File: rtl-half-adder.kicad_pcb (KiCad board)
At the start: 2 copper layers, 37 parts, among them Q1 Q_NPN_EBC, Q10 Q_NPN_EBC, Q11 Q_NPN_EBC, Q12 Q_NPN_EBC, Q13 Q_NPN_EBC, Q2 Q_NPN_EBC, Q3 Q_NPN_EBC, Q4 Q_NPN_EBC, Q5 Q_NPN_EBC, Q6 Q_NPN_EBC, Q7 Q_NPN_EBC, Q8 Q_NPN_EBC, Q9 Q_NPN_EBC, SW1 SW_DIP_x02

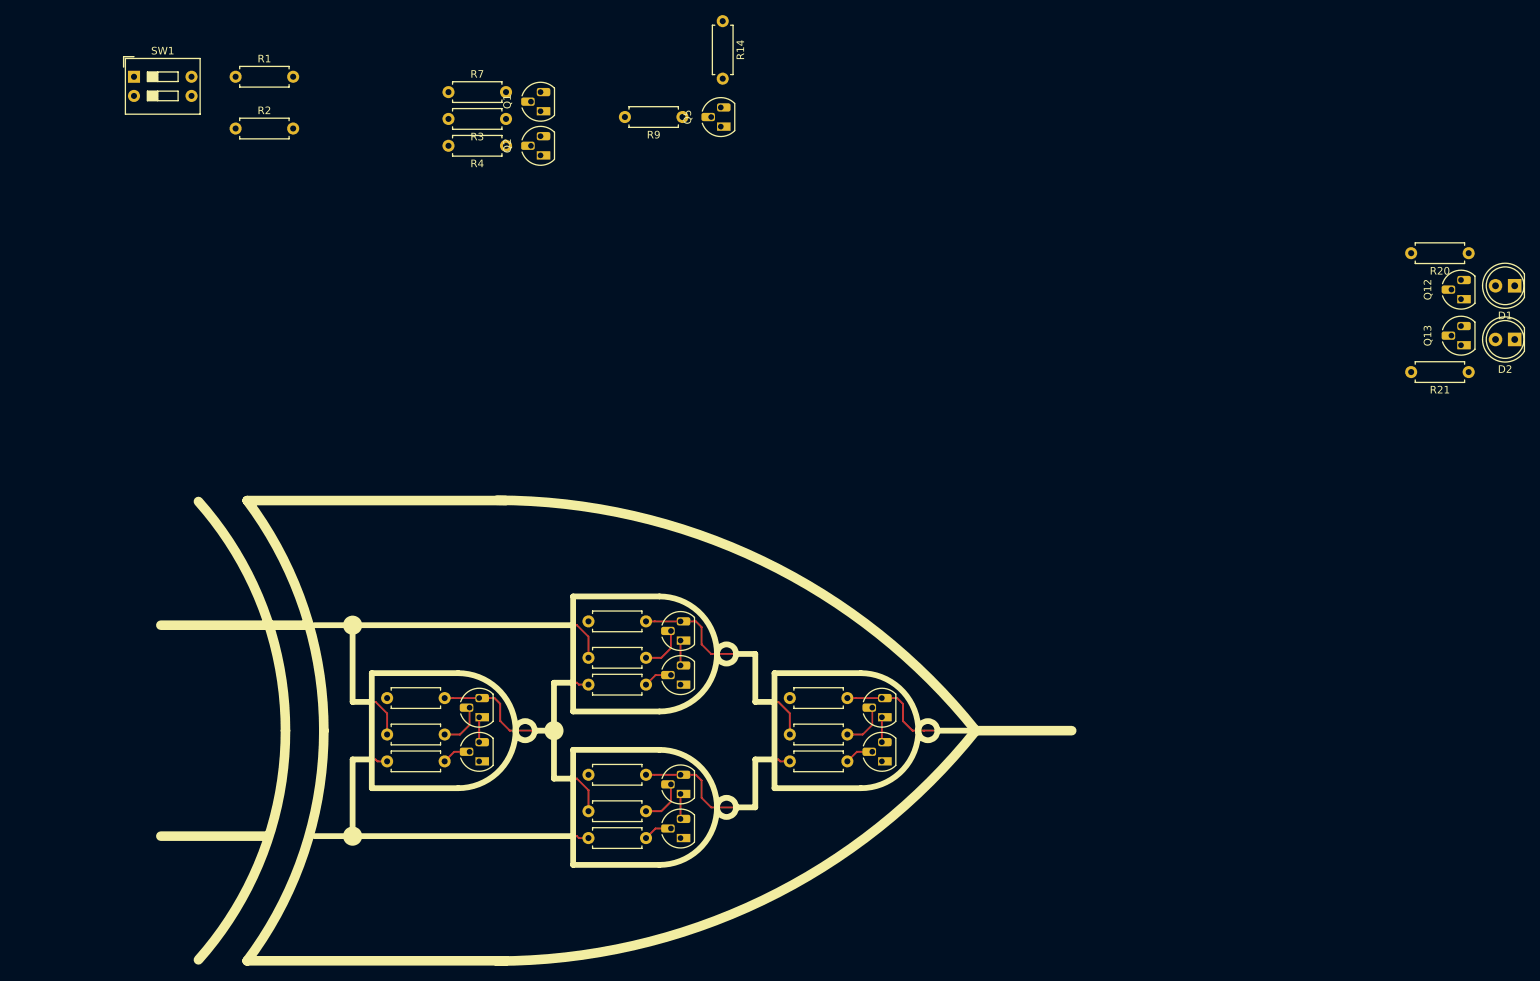
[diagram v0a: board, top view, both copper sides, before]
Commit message: through hole components and silk screen done
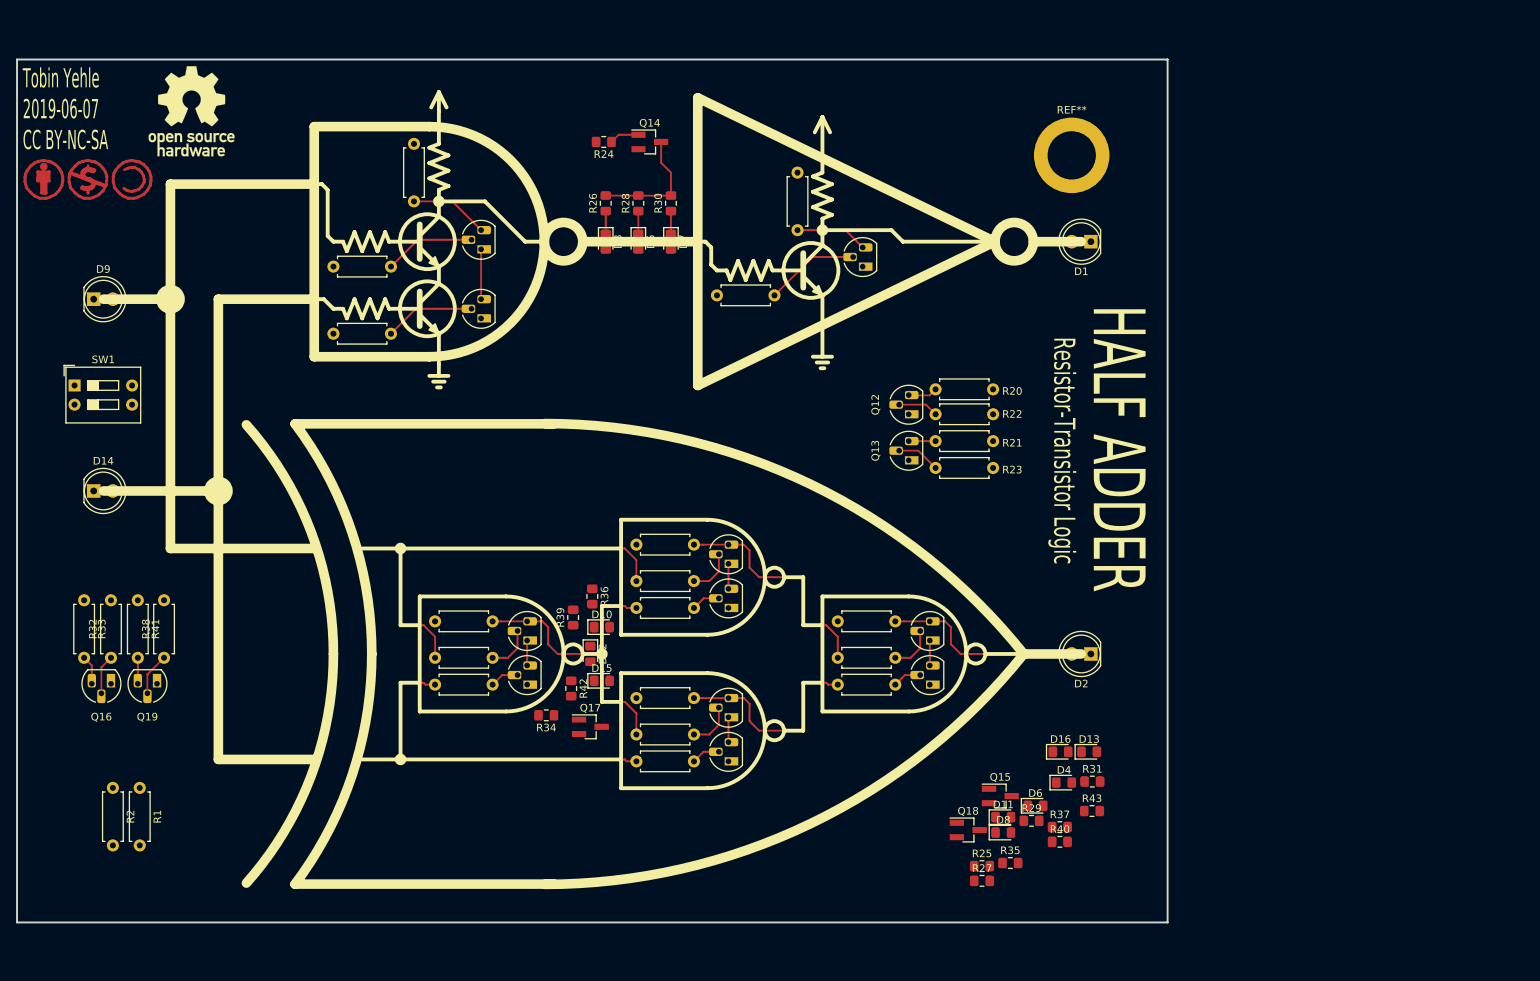
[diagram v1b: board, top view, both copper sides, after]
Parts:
- added D10: LED, LED_SMD:LED_0805_2012Metric_Pad1.15x1.40mm_HandSolder, F.Cu at (128.3, 113.3)
- added D11: LED, LED_SMD:LED_0805_2012Metric_Pad1.15x1.40mm_HandSolder, F.Cu at (181.4, 138.5)
- added D12: LED, LED_SMD:LED_0805_2012Metric_Pad1.15x1.40mm_HandSolder, F.Cu at (126.7, 116.8)
- added D13: LED, LED_SMD:LED_0805_2012Metric_Pad1.15x1.40mm_HandSolder, F.Cu at (192.8, 129.8)
- added D14: LED, LED_THT:LED_D5.0mm, F.Cu at (61.0, 95.2)
- added D15: LED, LED_SMD:LED_0805_2012Metric_Pad1.15x1.40mm_HandSolder, F.Cu at (128.3, 120.4)
- added D16: LED, LED_SMD:LED_0805_2012Metric_Pad1.15x1.40mm_HandSolder, F.Cu at (189.0, 129.8)
- added D3: LED, LED_SMD:LED_0805_2012Metric_Pad1.15x1.40mm_HandSolder, F.Cu at (128.8, 62.2)
- added D4: LED, LED_SMD:LED_0805_2012Metric_Pad1.15x1.40mm_HandSolder, F.Cu at (189.5, 133.9)
- added D5: LED, LED_SMD:LED_0805_2012Metric_Pad1.15x1.40mm_HandSolder, F.Cu at (133.1, 62.2)
- added D6: LED, LED_SMD:LED_0805_2012Metric_Pad1.15x1.40mm_HandSolder, F.Cu at (185.7, 136.9)
- added D7: LED, LED_SMD:LED_0805_2012Metric_Pad1.15x1.40mm_HandSolder, F.Cu at (137.4, 62.2)
- added D8: LED, LED_SMD:LED_0805_2012Metric_Pad1.15x1.40mm_HandSolder, F.Cu at (181.4, 140.5)
- added D9: LED, LED_THT:LED_D5.0mm, F.Cu at (61.0, 69.8)
- added Q14: Q_NPN_BEC, Package_TO_SOT_SMD:SOT-23_Handsoldering, F.Cu at (134.6, 49.0)
- added Q15: Q_NPN_BEC, Package_TO_SOT_SMD:SOT-23_Handsoldering, F.Cu at (181.0, 135.7)
- added Q16: Q_NPN_EBC, Package_TO_SOT_THT:TO-92_HandSolder, F.Cu at (63.2, 120.8)
- added Q17: Q_NPN_BEC, Package_TO_SOT_SMD:SOT-23_Handsoldering, F.Cu at (126.7, 126.5)
- added Q18: Q_NPN_BEC, Package_TO_SOT_SMD:SOT-23_Handsoldering, F.Cu at (176.8, 140.2)
- added Q19: Q_NPN_EBC, Package_TO_SOT_THT:TO-92_HandSolder, F.Cu at (69.3, 120.8)
- added R22: 10k, Resistor_THT:R_Axial_DIN0207_L6.3mm_D2.5mm_P7.62mm_Horizontal, F.Cu at (172.5, 85.1)
- added R23: 10k, Resistor_THT:R_Axial_DIN0207_L6.3mm_D2.5mm_P7.62mm_Horizontal, F.Cu at (172.5, 92.2)
- added R24: 10k, Resistor_SMD:R_0805_2012Metric_Pad1.15x1.40mm_HandSolder, F.Cu at (128.5, 49.0)
- added R25: 10k, Resistor_SMD:R_0805_2012Metric_Pad1.15x1.40mm_HandSolder, F.Cu at (178.6, 144.9)
- added R26: 68, Resistor_SMD:R_0805_2012Metric_Pad1.15x1.40mm_HandSolder, F.Cu at (128.8, 57.1)
- added R27: 68, Resistor_SMD:R_0805_2012Metric_Pad1.15x1.40mm_HandSolder, F.Cu at (178.6, 146.9)
- added R28: 68, Resistor_SMD:R_0805_2012Metric_Pad1.15x1.40mm_HandSolder, F.Cu at (133.1, 57.1)
- added R29: 68, Resistor_SMD:R_0805_2012Metric_Pad1.15x1.40mm_HandSolder, F.Cu at (185.2, 138.9)
- added R30: 68, Resistor_SMD:R_0805_2012Metric_Pad1.15x1.40mm_HandSolder, F.Cu at (137.4, 57.1)
- added R31: 68, Resistor_SMD:R_0805_2012Metric_Pad1.15x1.40mm_HandSolder, F.Cu at (193.2, 133.7)
- added R32: 10k, Resistor_THT:R_Axial_DIN0207_L6.3mm_D2.5mm_P7.62mm_Horizontal, F.Cu at (63.2, 117.3)
- added R33: 68, Resistor_THT:R_Axial_DIN0207_L6.3mm_D2.5mm_P7.62mm_Horizontal, F.Cu at (59.7, 109.7)
- added R34: 10k, Resistor_SMD:R_0805_2012Metric_Pad1.15x1.40mm_HandSolder, F.Cu at (120.9, 125.0)
- added R35: 10k, Resistor_SMD:R_0805_2012Metric_Pad1.15x1.40mm_HandSolder, F.Cu at (182.4, 144.5)
- added R36: 68, Resistor_SMD:R_0805_2012Metric_Pad1.15x1.40mm_HandSolder, F.Cu at (127.0, 109.2)
- added R37: 68, Resistor_SMD:R_0805_2012Metric_Pad1.15x1.40mm_HandSolder, F.Cu at (188.9, 139.8)
- added R38: 10k, Resistor_THT:R_Axial_DIN0207_L6.3mm_D2.5mm_P7.62mm_Horizontal, F.Cu at (70.3, 117.3)
- added R39: 68, Resistor_SMD:R_0805_2012Metric_Pad1.15x1.40mm_HandSolder, F.Cu at (124.5, 112.0)
- added R40: 68, Resistor_SMD:R_0805_2012Metric_Pad1.15x1.40mm_HandSolder, F.Cu at (188.9, 141.7)
- added R41: 68, Resistor_THT:R_Axial_DIN0207_L6.3mm_D2.5mm_P7.62mm_Horizontal, F.Cu at (66.8, 109.7)
- added R42: 68, Resistor_SMD:R_0805_2012Metric_Pad1.15x1.40mm_HandSolder, F.Cu at (124.2, 121.4)
- added R43: 68, Resistor_SMD:R_0805_2012Metric_Pad1.15x1.40mm_HandSolder, F.Cu at (193.2, 137.6)
- added REF**: OSHW-Logo_11.4x12mm_SilkScreen, Symbol:OSHW-Logo_11.4x12mm_SilkScreen, F.Cu at (73.9, 45.0)
- added REF**: MountingHole_6.4mm_M6_ISO14580_Pad, MountingHole:MountingHole_6.4mm_M6_ISO14580_Pad, F.Cu at (190.5, 50.8)
- added REF**: Symbol_CC-Attribution_CopperTop_Small, Symbol:Symbol_CC-Attribution_CopperTop_Small, F.Cu at (54.4, 54.0)
- added REF**: Symbol_CC-Noncommercial_CopperTop_Small, Symbol:Symbol_CC-Noncommercial_CopperTop_Small, F.Cu at (60.2, 54.0)
- added REF**: Symbol_CC-ShareAlike_CopperTop_Small, Symbol:Symbol_CC-ShareAlike_CopperTop_Small, F.Cu at (66.0, 54.0)
- R10, R11, R12, R13, R17, R18, R3, R4, R5, R6, R9: value 1k -> 10k
- moved R1 95.0 mm to (67.1, 134.6), turned to 270 degrees
- moved R2 88.8 mm to (63.5, 134.6), turned to 270 degrees
- moved Q12 74.7 mm to (168.9, 85.1)
- moved Q13 74.7 mm to (168.9, 91.2)
- moved D2 69.9 mm to (193.0, 116.8)
- moved R20 65.5 mm to (180.1, 81.8)
- moved R21 63.7 mm to (180.1, 88.6)
- moved D1 56.4 mm to (193.0, 62.2)
- moved SW1 41.6 mm to (58.4, 81.3)
- moved R4 29.2 mm to (100.3, 74.4)
- moved R9 26.6 mm to (151.1, 69.3)
- moved Q5 26.4 mm to (162.8, 65.5)
- moved R3 24.8 mm to (100.3, 65.5)
- moved Q2 23.0 mm to (112.3, 72.4)
- moved R14 22.4 mm to (154.2, 53.1)
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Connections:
- net Net-(Q1-Pad3) renamed NAND1
- net Net-(Q3-Pad3) renamed XOR1
- net Net-(Q6-Pad3) renamed XOR2
- net Net-(Q8-Pad3) renamed XOR3
- D1 pad 2: Net-(D1-Pad2) -> VCC
- D2 pad 2: Net-(D2-Pad2) -> VCC
- Q10 pad 3: Net-(Q10-Pad3) -> SUM
- Q12 pad 1: Net-(D1-Pad2) -> GND
- Q12 pad 3: VCC -> Net-(Q12-Pad3)
- Q13 pad 1: Net-(D2-Pad2) -> GND
- Q13 pad 2: Net-(Q10-Pad3) -> Net-(Q13-Pad2)
- Q13 pad 3: VCC -> Net-(Q13-Pad3)
- Q5 pad 3: Net-(Q12-Pad2) -> CARRY
- R1 pad 1: Net-(R1-Pad1) -> B
- R10 pad 2: Net-(R1-Pad1) -> A
- R13 pad 2: Net-(R13-Pad2) -> B
- R14 pad 2: Net-(Q12-Pad2) -> CARRY
- R19 pad 2: Net-(Q10-Pad3) -> SUM
- R2 pad 1: Net-(R13-Pad2) -> A
- R20 pad 2: GND -> Net-(Q12-Pad3)
- R21 pad 2: GND -> Net-(Q13-Pad3)
- R3 pad 2: Net-(R1-Pad1) -> A
- R4 pad 2: Net-(R13-Pad2) -> B
- R5 pad 2: Net-(R1-Pad1) -> A
- R6 pad 2: Net-(R13-Pad2) -> B
- SW1 pad 3: Net-(R13-Pad2) -> B
- SW1 pad 4: Net-(R1-Pad1) -> A
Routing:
- net Net-(R1-Pad1): track 51.9 -> 0.00 mm
- net Net-(R13-Pad2): track 45.3 -> 0.00 mm
- net A: track 0.00 -> 41.1 mm
- net B: track 0.00 -> 34.5 mm
- net SUM: track 0.00 -> 21.4 mm
- net Net-(Q10-Pad3): track 21.4 -> 0.00 mm
- net Net-(Q14-Pad3): track 0.00 -> 16.3 mm
- net XOR1: track 42.2 -> 29.3 mm
- net Net-(Q5-Pad2): track 0.00 -> 12.5 mm
- net Net-(Q1-Pad2): track 0.00 -> 12.1 mm
- net Net-(Q2-Pad2): track 0.00 -> 12.0 mm
- net NAND1: track 0.00 -> 10.5 mm
- net CARRY: track 0.00 -> 9.58 mm
- net XOR2: track 31.4 -> 24.6 mm
- net XOR3: track 28.0 -> 21.3 mm
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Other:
- board outline added: 152.4 x 114.3 mm
- board text added: "HALF ADDER"
- board text added: "Resistor-Transistor Logic"
- board text added: "Tobin Yehle 2019-06-07 CC BY-NC-SA"

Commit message: update footprints for smd leds
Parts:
- D10, D11, D12, D13, D15, D16, D3, D4, D5, D6, D7, D8: footprint LED_SMD:LED_0805_2012Metric_Pad1.15x1.40mm_HandSolder -> --Project:LED_1206_3216Metric_ReverseMount_Hole1.8x2.4mm

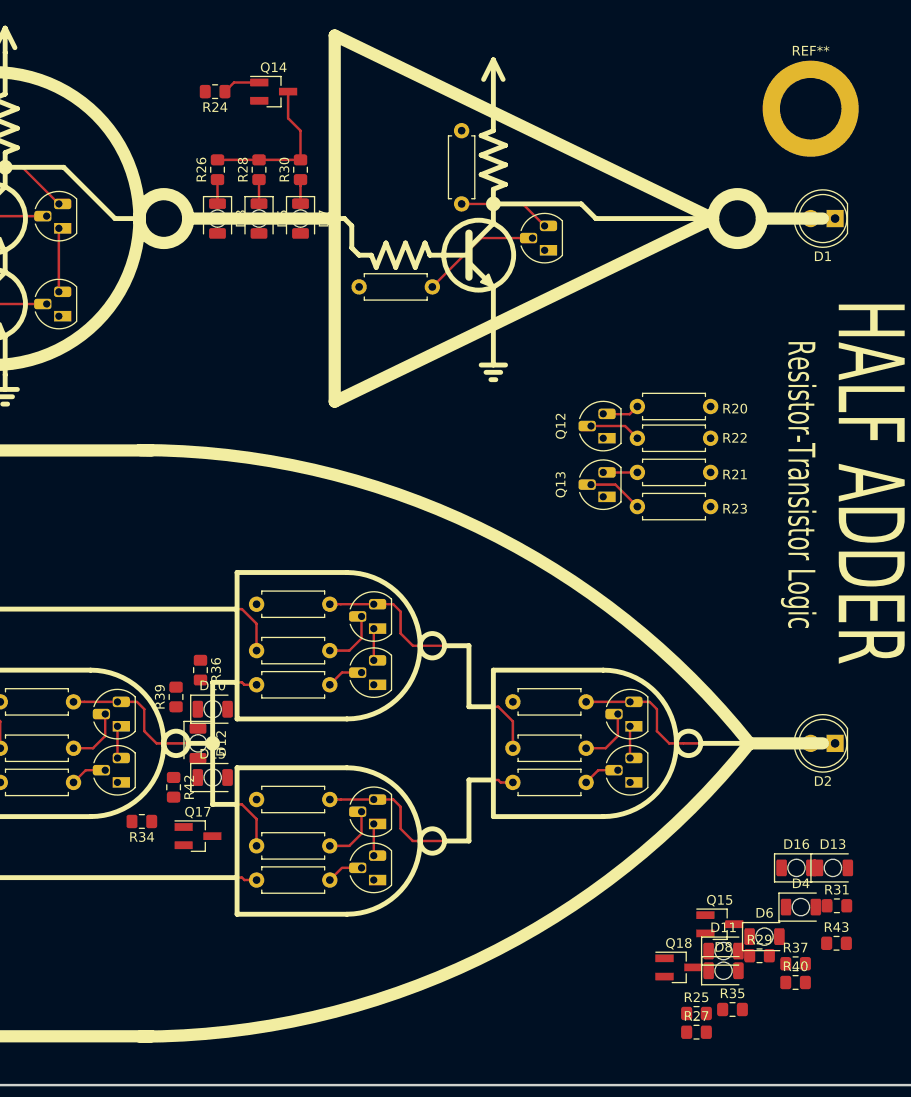
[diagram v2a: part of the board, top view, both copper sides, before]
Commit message: inter gate led layout done
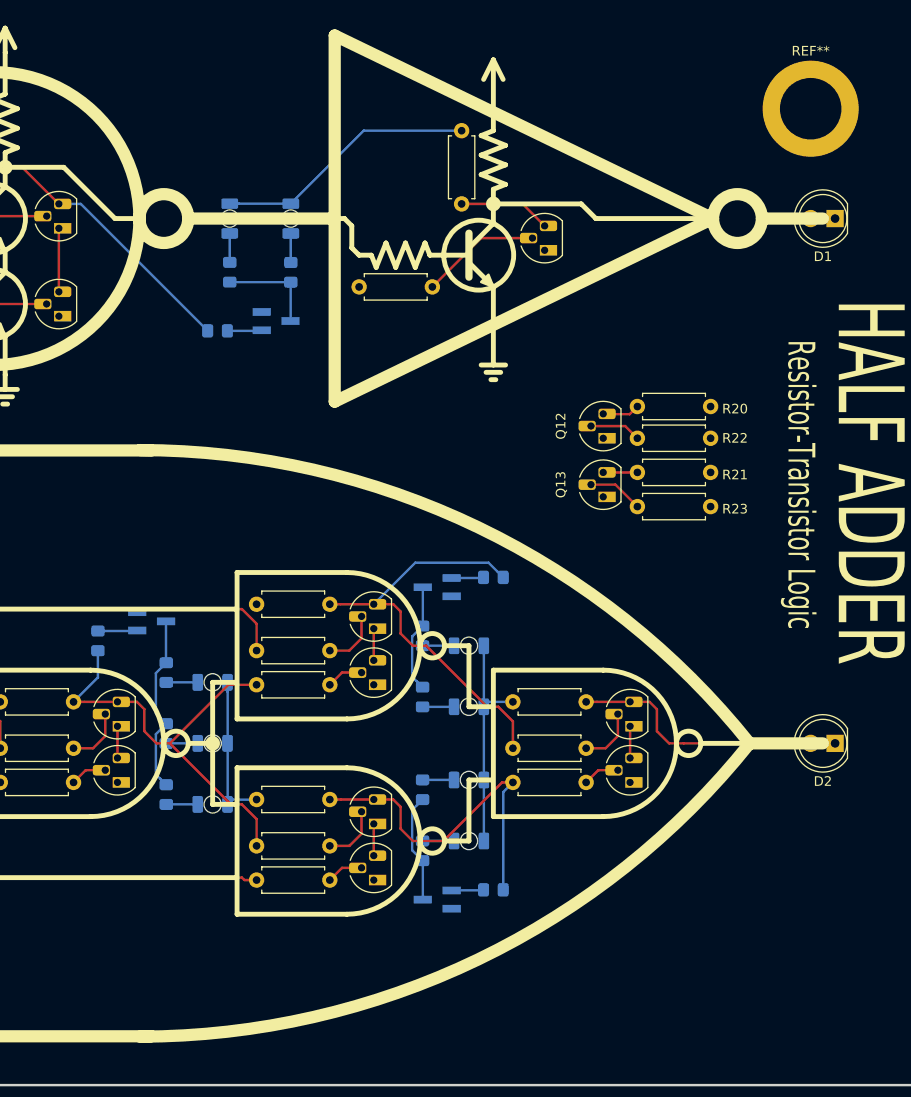
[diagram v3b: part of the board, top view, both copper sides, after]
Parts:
- removed D16, D7, D8: LED, --Project:LED_1206_3216Metric_ReverseMount_Hole1.8x2.4mm
- removed R30, R31, R43: 68, Resistor_SMD:R_0805_2012Metric_Pad1.15x1.40mm_HandSolder
- D10, D11, D12, D13, D15, D3, D4, D5, D6, Q14, Q15, Q17, Q18, R24, R25, R26, R27, R28, R29, R34, R35, R36, R37, R39, R40, R42: moved to B.Cu
- moved R27 50.1 mm to (150.1, 105.7), turned to 90 degrees
- moved R25 50.1 mm to (157.5, 99.6)
- moved Q15 45.8 mm to (151.6, 100.6), turned to 180 degrees
- moved R29 44.2 mm to (150.1, 112.0), turned to 90 degrees
- moved D4 44.0 mm to (154.9, 106.7)
- moved R40 43.7 mm to (150.1, 121.7), turned to 270 degrees
- moved R37 40.6 mm to (150.1, 128.0), turned to 270 degrees
- moved D13 39.0 mm to (154.9, 120.7)
- moved D6 39.0 mm to (154.9, 113.0)
- moved D11 28.9 mm to (154.9, 127.0)
- moved R35 27.8 mm to (157.5, 132.1)
- moved Q18 26.1 mm to (151.6, 133.1), turned to 180 degrees
- moved R24 24.9 mm to (128.8, 73.9)
- moved Q14 23.9 mm to (134.9, 72.9)
- moved Q17 22.9 mm to (121.9, 104.1)
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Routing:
- net VCC: track 0.00 -> 66.8 mm
- net NAND1: track 10.5 -> 31.4 mm
- net XOR2: track 24.6 -> 44.1 mm
- net Net-(Q17-Pad3): track 0.00 -> 18.8 mm
- net XOR1: track 29.3 -> 46.2 mm
- net XOR3: track 21.3 -> 36.3 mm
- net Net-(Q18-Pad3): track 0.00 -> 11.3 mm
- net Net-(Q15-Pad3): track 0.00 -> 11.3 mm
- net Net-(Q14-Pad3): track 16.3 -> 10.4 mm
- net Net-(Q17-Pad1): track 0.00 -> 4.11 mm
- net Net-(Q15-Pad1): track 0.00 -> 3.34 mm
- net Net-(Q18-Pad1): track 0.00 -> 3.34 mm
- net Net-(D15-Pad1): track 0.00 -> 3.28 mm
- net Net-(D12-Pad1): track 0.00 -> 3.28 mm
- net Net-(D10-Pad1): track 0.00 -> 3.28 mm
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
